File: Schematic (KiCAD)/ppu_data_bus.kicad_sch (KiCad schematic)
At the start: 72 parts, among them J65 Reg 4 D-Latch N, J68 Counter 4 Reset CL3

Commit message: Schematic Updates:  - Added all 10-bit CHR banking registers $5120 - $512B, including where all 10 bits come from when written.  - Added 8-bit CHR bank register $5202, which is the bank used when rendering the V-Split region.    + V-Split seems to always be 8-bit, 8kB bank regardless of CHR mode.  The wiki doesn't say that and I don't know for sure.  - Added decoding logic that activates the correct CHR bank for CHR A10, A11, A12 (corresponding to columns AV, AW, AX).  - Noted, AX15 activates $5202 CHR Bank for V-Split region.  AX16 activates CHR Bank from data stored in ExRAM for extended attributes.  Therefore, AX15 driven by AT1 High means we specifically are in v-split region, and not extended attribute mode.  With this knowledge, backtracking up the chain from AT1 to N14 sheds very useful insight what the 3-bit shift register at N11/N12/N13 is doing.  We now know that N14 goes low specifically for pattern table fetches when rendering the V-split region, and does not appear dual-purposed for extended attribute fetch sequencing.  This may seem rather subtle or unimportant, but it is a good advancement for higher level understanding what that mysterious shift register might be doing.
SVG Trace Updates:
 - Registers $5120, 5121, 5122, 5123 (first 4 CHR bank register), the outputs were labeled in reverse order.
 - Register $5130 (highest CHR bank bits), the outputs were labeled with backwards polarity.  The error was not having taken into account that the CPU data bus input to the latches came already inverted to begin with.
 - Still wrong: Cell AV7, 2-input NAND gate.  One of the inputs is missing and it logically should be driven by AS19 like the 4 cells to its direct right.  I can't quite make out how it makes that connection.
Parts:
- removed B100, B99, E47, F32, G20, H90: NOR_2, symbol MMC5:NOR_2
- removed B103, B105, C32, C34, C35, C37, C39, C40, E46, E48, F14, F15, F17, F22, F23, F24, F26, F27, F33, F34, F35, F36, F7.1, F8, F9, G95, H100, H101, H102, H103, H108, H89, H91, H99: INVERT, symbol MMC5:INVERT
- removed C31(a), C31(b): D-FF No Reset, symbol MMC5:D-FF_No_Reset
- removed C33, C38: NOR_3, symbol MMC5:NOR_3
- removed C36, C41: Unk 2to2, symbol MMC5:UNKNOWN_2to2
- removed E45, H92: NAND_2, symbol MMC5:NAND_2
- removed E53, J68: Counter 4 Reset CL3, symbol MMC5:Counter_4_Reset_CL3
- removed E68, F37, G85, J65: Reg 4 D-Latch N, symbol MMC5:Reg_4_D-Latch_N
- removed F10, F11, F12, F13, G93, G94, G98, G99: NAND_3, symbol MMC5:NAND_3
- removed F16, G97: NAND_4, symbol MMC5:NAND_4
- removed F18, F19, F20, F21, H104, H105, H106, H107: AOI_2, symbol MMC5:AOI_2
- added BH1, BH10, BH17, BH19, BH2, BH21, BH23, BH25, BH26, BH27, BH9, BK12, BK16, BK20, BK24, BK28, BK32, BK36, BK8, BL28, BL30, BL31, BL38, BL39, BL40, BL45: INVERT, symbol MMC5:INVERT
- added BH11, BH3: NAND_5, symbol MMC5:NAND_5
- added BH12, BH13, BH14, BH15, BH16, BH4, BH5, BH6, BH7, BH8, BK10, BK13, BK14, BK17, BK18, BK21, BK22, BK25, BK26, BK29, BK30, BK33, BK34, BK37, BK38, BK40, BK41, BK42, BK43, BK9, BL12, BL13, BL14, BL15, BL16, BL17, BL18, BL19, BL35, BL36, BL41, S2: NAND_2, symbol MMC5:NAND_2
- added BH18, BH20, BH22, BH24, BK11, BK15, BK19, BK23, BK27, BK31, BK35, BK7, BL32, BL37, BL42: NAND_3, symbol MMC5:NAND_3
- added BK1, BK39, BK44, BL1, BL10, BL2, BL3, BL34, BL4, BL46, BL5, BL6, BL7, S1: BUFFER, symbol MMC5:BUFFER
- added BL29: NAND_4, symbol MMC5:NAND_4
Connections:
- new net: BK24. (X), BK25. (X)
- new net: BK23. (X), BK24. (X)
- new net: BL12. (X), BL13. (X), BL14. (X), BL15. (X), BL16. (X), BL17. (X), BL18. (X), BL19. (X), BL31. (X)
- new net: BK15. (X), BL14. (X)
- new net: BL14. (X), BL2. (X)
- new net: BK10. (X), BK14. (X), BK18. (X), BK22. (X), BK26. (X), BK30. (X), BK34. (X), BK38. (X), BL39. (X)
- new net: BL39. (X), BL42. (X)
- new net: BL41. (X), BL45. (X)
- new net: BL41. (X), BL42. (X)
- new net: BH21. (X), BH22. (X)
- new net: BH12. (X), BH21. (X), BH4. (X)
- new net: BK8. (X), BK9. (X)
- new net: BK7. (X), BK8. (X)
- new net: BL31. (X), BL32. (X)
- new net: BH19. (X), BH20. (X)
- new net: BH14. (X), BH19. (X), BH6. (X)
- new net: BK25. (X), BK26. (X)
- new net: BH13. (X), BH23. (X), BH5. (X)
- new net: BH11. (X), BH13. (X)
- new net: BK35. (X), BL19. (X)
- new net: BL19. (X), BL7. (X)
- new net: BK10. (X), BK9. (X)
- new net: BL34. (X), BL35. (X), BL37. (X)
- new net: BL35. (X), BL40. (X)
- new net: BL29. (X), BL35. (X)
- new net: BK7. (X), BL12. (X)
- new net: BK1. (X), BL12. (X)
- new net: S1. (X), S2. (X)
- new net: BK15. (X), BK23. (X), BK31. (X), BK42. (X), BK7. (X)
- new net: BK15. (X), BK23. (X), BK31. (X), BK43. (X), BK7. (X)
- new net: BK31. (X), BL18. (X)
- new net: BK31. (X), BK32. (X)
- new net: BK37. (X), BK38. (X)
- new net: BK36. (X), BK37. (X)
- new net: BK15. (X), BK16. (X)
- new net: BK16. (X), BK17. (X)
- new net: BL45. (X), BL46. (X)
- new net: BH18. (X), BH20. (X), BH26. (X)
- new net: BH18. (X), BH20. (X), BH22. (X), BH24. (X), BH25. (X)
- new net: BH17. (X), BH18. (X)
- new net: BH18. (X), BH22. (X), BH27. (X)
- new net: BH15. (X), BH17. (X), BH7. (X)
- new net: BH11. (X), BH15. (X)
- new net: BK29. (X), BK30. (X)
- new net: BK28. (X), BK29. (X)
- new net: BK11. (X), BK19. (X), BK27. (X), BK35. (X), BK40. (X)
- new net: BK39. (X), BK40. (X), BK42. (X)
- new net: BH1. (X), BH2. (X)
- new net: BH2. (X), BH3. (X)
- new net: BK23. (X), BL16. (X)
- new net: BK11. (X), BK19. (X), BK27. (X), BK35. (X), BK41. (X)
- new net: BK11. (X), BL13. (X)
- new net: BK11. (X), BK12. (X)
- new net: BK21. (X), BK22. (X)
- new net: BH1. (X), BK41. (X)
- new net: BK12. (X), BK13. (X)
- new net: BK13. (X), BK14. (X)
- new net: BH10. (X), BH9. (X)
- new net: BH10. (X), BH11. (X)
- new net: BK39. (X), BL30. (X)
- new net: BL1. (X), BL13. (X)
- new net: BL28. (X), BL29. (X), BL37. (X)
- new net: BL18. (X), BL6. (X)
- new net: BL10. (X), BL34. (X)
- new net: BL15. (X), BL3. (X)
- new net: BL29. (X), BL30. (X)
- new net: BK27. (X), BL17. (X)
- new net: BK27. (X), BK28. (X)
- new net: BH23. (X), BH24. (X)
- new net: BH20. (X), BH24. (X), BH27. (X), S1. (X)
- new net: BK41. (X), BK43. (X), BK44. (X)
- new net: BL36. (X), BL37. (X)
- new net: BL37. (X), BL38. (X), BL42. (X)
- new net: BK20. (X), BK21. (X)
- new net: BK33. (X), BK34. (X)
- new net: BK44. (X), BL38. (X)
- new net: BH11. (X), BH16. (X)
- new net: BL17. (X), BL5. (X)
- new net: BK35. (X), BK36. (X)
- new net: BL16. (X), BL4. (X)
- new net: BK19. (X), BL15. (X)
- new net: BH3. (X), BH5. (X)
- new net: BH3. (X), BH8. (X)
- new net: BH3. (X), BH4. (X)
- new net: BH3. (X), BH7. (X)
- new net: BH3. (X), BH6. (X)
- new net: BK17. (X), BK18. (X)
- new net: BH9. (X), BK43. (X)
- new net: BK32. (X), BK33. (X)
- new net: BK19. (X), BK20. (X)
- new net: BH11. (X), BH14. (X)
- new net: BH11. (X), BH12. (X)
- new net +$5106.0_Fill_Mode_Tile{L11}: BK1. (X)
- new net +$5106.1_Fill_Mode_Tile{L12}: BL1. (X)
- new net +$5106.2_Fill_Mode_Tile{L14}: BL2. (X)
- new net +$5106.3_Fill_Mode_Tile{L13}: BL3. (X)
- new net +$5106.4_Fill_Mode_Tile{L18}: BL4. (X)
- new net +$5106.5_Fill_Mode_Tile{L17}: BL5. (X)
- new net +$5106.6_Fill_Mode_Tile{L16}: BL6. (X)
- new net +$5106.7_Fill_Mode_Tile{L15}: BL7. (X)
- new net +$5107.0_Fill_Mode_Color{BL8}: BK42. (X)
- new net +$5107.1_Fill_Mode_Color{BL9}: BK40. (X)
- new net +ExRAM_Nametable_Access{A9}: BL46. (X)
- new net +ExRAM_Read_D6_Latch{BJ11}: BH16. (X)
- new net +ExRAM_Read_D7_Latch{BJ11}: BH8. (X)
- new net +Fill_Mode_Nametable_Access{BL33}: BL29. (X), BL32. (X)
- new net +PPU_Fetch_Count.0{S10}: S2. (X)
- new net +PPU_Fetch_Count.1{S13}: S2. (X)
- new net +V-Split_Scanline_Counter.4{T22}: BH22. (X), BH24. (X), BH26. (X)
- new net ExRAM_D0_Read{BJ12(a)}: BH15. (X), BK10. (X)
- new net ExRAM_D1_Read{BJ12(b)}: BH7. (X), BK14. (X)
- new net ExRAM_D2_Read{BJ12(c)}: BH14. (X), BK18. (X)
- new net ExRAM_D3_Read{BJ12(d)}: BH6. (X), BK22. (X)
- new net ExRAM_D4_Read{BJ12(e)}: BH13. (X), BK26. (X)
- new net ExRAM_D5_Read{BJ12(f)}: BH5. (X), BK30. (X)
- new net ExRAM_D6_Read{BJ12(g)}: BH12. (X), BK34. (X)
- new net ExRAM_D7_Read{BJ12(h)}: BH4. (X), BK38. (X)
- new net PPU_D0_OUT_PIN: BK9. (X)
- new net PPU_D1_OUT_PIN: BK13. (X)
- new net PPU_D2_OUT_PIN: BK17. (X)
- new net PPU_D3_OUT_PIN: BK21. (X)
- new net PPU_D4_OUT_PIN: BK25. (X)
- new net PPU_D5_OUT_PIN: BK29. (X)
- new net PPU_D6_OUT_PIN: BK33. (X)
- new net PPU_D7_OUT_PIN: BK37. (X)
- new net PPU_RW_Mode_%0x_Access{BL48}: BL42. (X)
- new net V-Split_Side_Latched{BL43}: BH16. (X), BH25. (X), BH8. (X), BL29. (X), BL32. (X), BL36. (X), BL41. (X)
- new net /ExRAM_Mode_%01{BL49}: BL36. (X), BL40. (X)
- new net /PPU_Attribute_Access{BL25}: BL28. (X), BL32. (X)
- new net /Scanline_Counter_Reset{Z25}: BL10. (X)
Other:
- note added: "/Extended Attributes Enabled"
- note removed: "$5000 Register Pulse 1 Duty Envelope Volume"
- note removed: "$5004 Register Pulse 2 Duty Envelope Volume"
- note removed: "Bit 0 is internally bypassed."
- note removed: "Pulse 1 Duty Cycle Counter"
- note removed: "Pulse 1 Envelope/Volume Multiplexing"
- note removed: "Pulse 2 Duty Cycle Counter"
- note removed: "Pulse 2 Envelope/Volume Multiplexing"

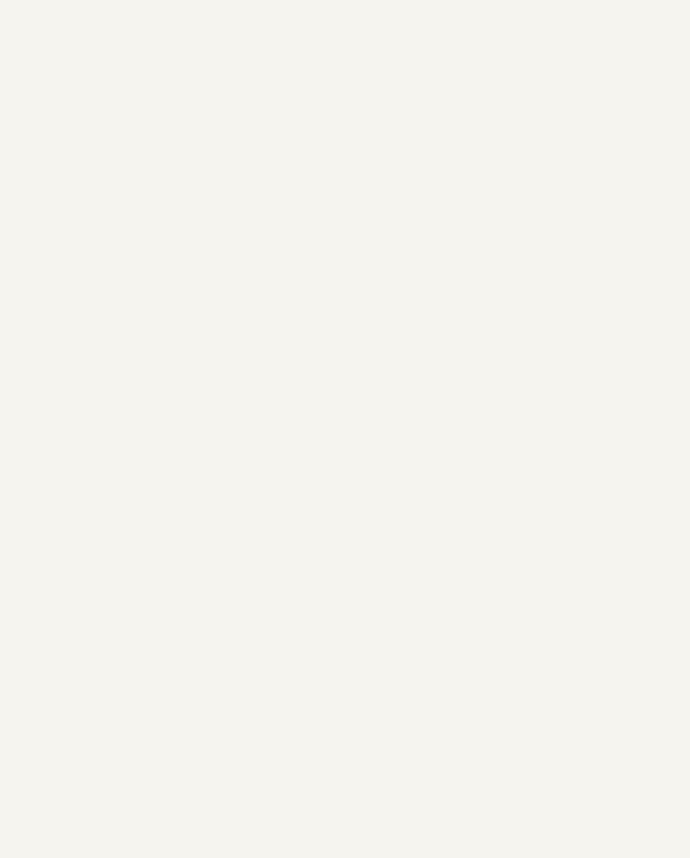
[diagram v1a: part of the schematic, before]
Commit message: - All cells in the left and center areas have now been added into the schematics.  - Changed naming of the PDF files; I was accidentally writing over furrtek's original with my new PDF.
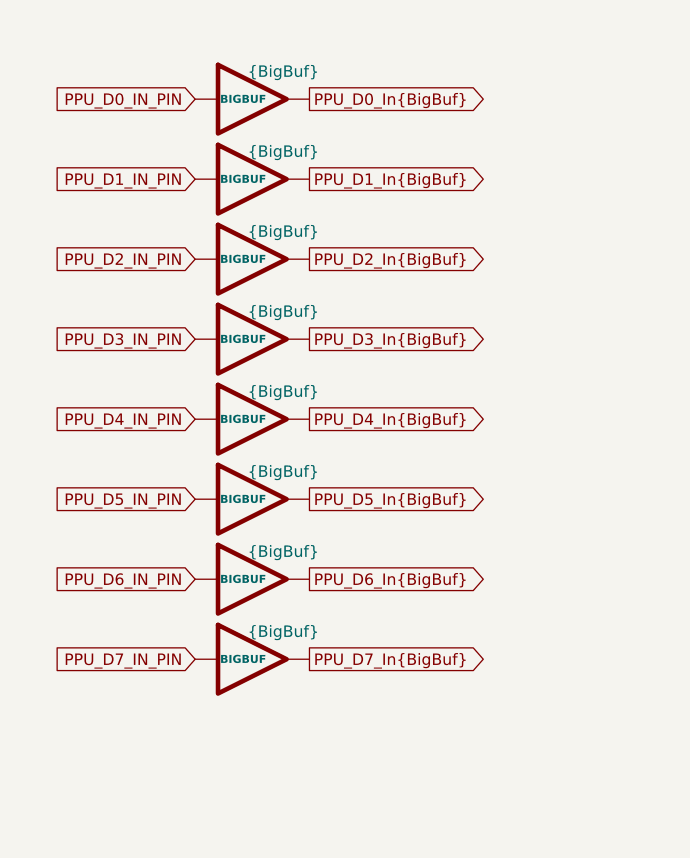
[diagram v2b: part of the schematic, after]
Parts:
- added {BigBuf} (x8): BIGBUF, symbol MMC5:BIGBUF
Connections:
- net at BK24. (X): now also BK23. (X); no longer BK25. (X)
- net at BK23. (X): now also BL16. (X); no longer BK24. (X)
- net at BL14. (X): now also BL2. (X); no longer BK15. (X)
- net at BL45. (X): now also BL46. (X); no longer BL41. (X)
- net at BH21. (X): now also BH12. (X), BH4. (X); no longer BH22. (X)
- net at BK8. (X): now also BK7. (X); no longer BK9. (X)
- net at BK7. (X): now also BK15. (X), BK23. (X), BK31. (X), BK43. (X); no longer BK8. (X)
- net at BH19. (X): now also BH14. (X), BH6. (X); no longer BH20. (X)
- net at BH11. (X): now also BH12. (X); no longer BH13. (X)
- net at BL19. (X): now also BL7. (X); no longer BK35. (X)
- net at BL35. (X): now also BL29. (X); no longer BL40. (X)
- net at BL12. (X): now also BK1. (X); no longer BK7. (X)
- net at S1. (X): now also BH20. (X), BH24. (X), BH27. (X); no longer S2. (X)
- net at BK31. (X): now also BK32. (X); no longer BL18. (X)
- net at BK32. (X): now also BK33. (X); no longer BK31. (X)
- net at BK36. (X): now also BK35. (X); no longer BK37. (X)
- net at BH18. (X): now also BH22. (X), BH27. (X); no longer BH17. (X)
- net at BK28. (X): now also BK27. (X); no longer BK29. (X)
- net at BH2. (X): now also BH3. (X); no longer BH1. (X)
- net at BH3. (X): now also BH6. (X); no longer BH2. (X)
- net at BL16. (X): now also BL4. (X); no longer BK23. (X)
- net at BK11. (X): now also BK12. (X); no longer BL13. (X)
- net at BK12. (X): now also BK13. (X); no longer BK11. (X)
- net at BH10. (X): now also BH11. (X); no longer BH9. (X)
- net at BL15. (X): now also BK19. (X); no longer BL3. (X)
- net at BL17. (X): now also BL5. (X); no longer BK27. (X)
- net at BL37. (X): now also BL38. (X), BL42. (X); no longer BL36. (X)
- net at BK20. (X): now also BK19. (X); no longer BK21. (X)
- new net: BK24. (X), BK25. (X)
- new net: BL12. (X), BL13. (X), BL14. (X), BL15. (X), BL16. (X), BL17. (X), BL18. (X), BL19. (X), BL31. (X)
- new net: BK15. (X), BL14. (X)
- new net: BK10. (X), BK14. (X), BK18. (X), BK22. (X), BK26. (X), BK30. (X), BK34. (X), BK38. (X), BL39. (X)
- new net: BL41. (X), BL45. (X)
- new net: BL41. (X), BL42. (X)
- new net: BH21. (X), BH22. (X)
- new net: BK8. (X), BK9. (X)
- new net: BH19. (X), BH20. (X)
- new net: BK25. (X), BK26. (X)
- new net: BH13. (X), BH23. (X), BH5. (X)
- new net: BH11. (X), BH13. (X)
- new net: BK35. (X), BL19. (X)
- new net: BK10. (X), BK9. (X)
- new net: BL34. (X), BL35. (X), BL37. (X)
- new net: BL35. (X), BL40. (X)
- new net: BK7. (X), BL12. (X)
- new net: S1. (X), S2. (X)
- new net: BK15. (X), BK23. (X), BK31. (X), BK42. (X), BK7. (X)
- new net: BK31. (X), BL18. (X)
- new net: BK37. (X), BK38. (X)
- new net: BK36. (X), BK37. (X)
- new net: BH18. (X), BH20. (X), BH26. (X)
- new net: BH18. (X), BH20. (X), BH22. (X), BH24. (X), BH25. (X)
- new net: BH17. (X), BH18. (X)
- new net: BH15. (X), BH17. (X), BH7. (X)
- new net: BH11. (X), BH15. (X)
- new net: BK29. (X), BK30. (X)
- new net: BK28. (X), BK29. (X)
- new net: BK11. (X), BK19. (X), BK27. (X), BK35. (X), BK40. (X)
- new net: BK39. (X), BK40. (X), BK42. (X)
- new net: BH1. (X), BH2. (X)
- new net: BK11. (X), BK19. (X), BK27. (X), BK35. (X), BK41. (X)
- new net: BK11. (X), BL13. (X)
- new net: BK21. (X), BK22. (X)
- new net: BK13. (X), BK14. (X)
- new net: BH10. (X), BH9. (X)
- new net: BL28. (X), BL29. (X), BL37. (X)
- new net: BL15. (X), BL3. (X)
- new net: BK27. (X), BL17. (X)
- new net: BK41. (X), BK43. (X), BK44. (X)
- new net: BL36. (X), BL37. (X)
- new net: BK20. (X), BK21. (X)
- new net: BK33. (X), BK34. (X)
- new net: BH11. (X), BH16. (X)
- new net: BH3. (X), BH5. (X)
- new net: BH3. (X), BH8. (X)
- new net: BH3. (X), BH4. (X)
- new net: BH3. (X), BH7. (X)
- new net: BK17. (X), BK18. (X)
- new net: BH11. (X), BH14. (X)
- new net PPU_D0_IN_PIN: {BigBuf}. (X)
- new net PPU_D0_In{BigBuf}: {BigBuf}. (X)
- new net PPU_D1_IN_PIN: {BigBuf}. (X)
- new net PPU_D1_In{BigBuf}: {BigBuf}. (X)
- new net PPU_D2_IN_PIN: {BigBuf}. (X)
- new net PPU_D2_In{BigBuf}: {BigBuf}. (X)
- new net PPU_D3_IN_PIN: {BigBuf}. (X)
- new net PPU_D3_In{BigBuf}: {BigBuf}. (X)
- new net PPU_D4_IN_PIN: {BigBuf}. (X)
- new net PPU_D4_In{BigBuf}: {BigBuf}. (X)
- new net PPU_D5_IN_PIN: {BigBuf}. (X)
- new net PPU_D5_In{BigBuf}: {BigBuf}. (X)
- new net PPU_D6_IN_PIN: {BigBuf}. (X)
- new net PPU_D6_In{BigBuf}: {BigBuf}. (X)
- new net PPU_D7_IN_PIN: {BigBuf}. (X)
- new net PPU_D7_In{BigBuf}: {BigBuf}. (X)

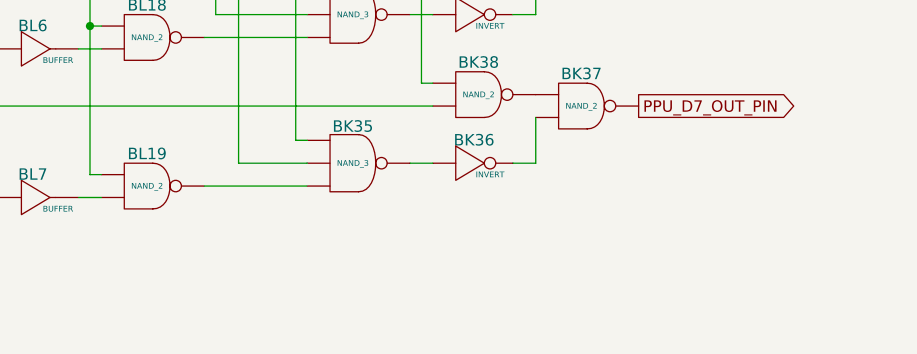
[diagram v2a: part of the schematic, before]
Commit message: - All known gates and traces are now accounted for in the schematics!  :)
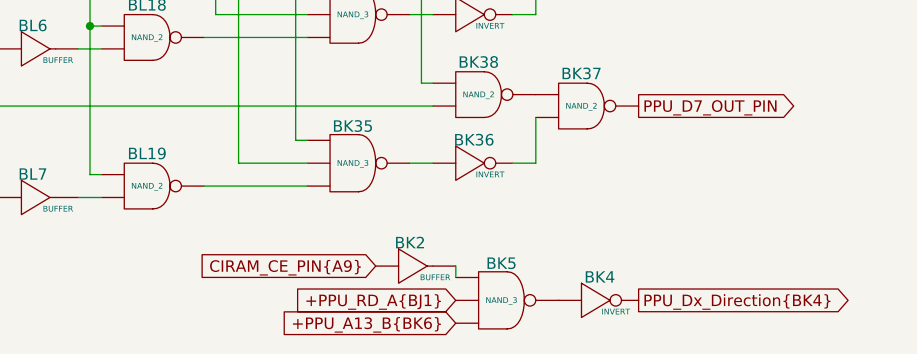
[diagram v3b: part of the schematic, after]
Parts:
- added BK2: BUFFER, symbol MMC5:BUFFER
- added BK4: INVERT, symbol MMC5:INVERT
- added BK5: NAND_3, symbol MMC5:NAND_3
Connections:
- net at BK24. (X): now also BK23. (X); no longer BK25. (X)
- net at BK23. (X): now also BL16. (X); no longer BK24. (X)
- net at BL14. (X): now also BL2. (X); no longer BK15. (X)
- net at BL45. (X): now also BL46. (X); no longer BL41. (X)
- net at BH21. (X): now also BH12. (X), BH4. (X); no longer BH22. (X)
- net at BK8. (X): now also BK7. (X); no longer BK9. (X)
- net at BK7. (X): now also BK15. (X), BK23. (X), BK31. (X), BK43. (X); no longer BK8. (X)
- net at BH19. (X): now also BH14. (X), BH6. (X); no longer BH20. (X)
- net at BH11. (X): now also BH12. (X); no longer BH13. (X)
- net at BL19. (X): now also BL7. (X); no longer BK35. (X)
- net at BL35. (X): now also BL29. (X); no longer BL40. (X)
- net at BL12. (X): now also BK1. (X); no longer BK7. (X)
- net at S1. (X): now also BH20. (X), BH24. (X), BH27. (X); no longer S2. (X)
- net at BK31. (X): now also BK32. (X); no longer BL18. (X)
- net at BK32. (X): now also BK33. (X); no longer BK31. (X)
- net at BK36. (X): now also BK35. (X); no longer BK37. (X)
- net at BH18. (X): now also BH22. (X), BH27. (X); no longer BH17. (X)
- net at BK28. (X): now also BK27. (X); no longer BK29. (X)
- net at BH2. (X): now also BH3. (X); no longer BH1. (X)
- net at BH3. (X): now also BH6. (X); no longer BH2. (X)
- net at BL16. (X): now also BL4. (X); no longer BK23. (X)
- net at BK11. (X): now also BK12. (X); no longer BL13. (X)
- net at BK12. (X): now also BK13. (X); no longer BK11. (X)
- net at BH10. (X): now also BH11. (X); no longer BH9. (X)
- net at BL15. (X): now also BK19. (X); no longer BL3. (X)
- net at BL17. (X): now also BL5. (X); no longer BK27. (X)
- net at BL37. (X): now also BL38. (X), BL42. (X); no longer BL36. (X)
- net at BK20. (X): now also BK19. (X); no longer BK21. (X)
- new net: BK24. (X), BK25. (X)
- new net: BL12. (X), BL13. (X), BL14. (X), BL15. (X), BL16. (X), BL17. (X), BL18. (X), BL19. (X), BL31. (X)
- new net: BK15. (X), BL14. (X)
- new net: BK10. (X), BK14. (X), BK18. (X), BK22. (X), BK26. (X), BK30. (X), BK34. (X), BK38. (X), BL39. (X)
- new net: BL41. (X), BL45. (X)
- new net: BL41. (X), BL42. (X)
- new net: BH21. (X), BH22. (X)
- new net: BK8. (X), BK9. (X)
- new net: BK4. (X), BK5. (X)
- new net: BK2. (X), BK5. (X)
- new net: BH19. (X), BH20. (X)
- new net: BK25. (X), BK26. (X)
- new net: BH13. (X), BH23. (X), BH5. (X)
- new net: BH11. (X), BH13. (X)
- new net: BK35. (X), BL19. (X)
- new net: BK10. (X), BK9. (X)
- new net: BL34. (X), BL35. (X), BL37. (X)
- new net: BL35. (X), BL40. (X)
- new net: BK7. (X), BL12. (X)
- new net: S1. (X), S2. (X)
- new net: BK15. (X), BK23. (X), BK31. (X), BK42. (X), BK7. (X)
- new net: BK31. (X), BL18. (X)
- new net: BK37. (X), BK38. (X)
- new net: BK36. (X), BK37. (X)
- new net: BH18. (X), BH20. (X), BH26. (X)
- new net: BH18. (X), BH20. (X), BH22. (X), BH24. (X), BH25. (X)
- new net: BH17. (X), BH18. (X)
- new net: BH15. (X), BH17. (X), BH7. (X)
- new net: BH11. (X), BH15. (X)
- new net: BK29. (X), BK30. (X)
- new net: BK28. (X), BK29. (X)
- new net: BK11. (X), BK19. (X), BK27. (X), BK35. (X), BK40. (X)
- new net: BK39. (X), BK40. (X), BK42. (X)
- new net: BH1. (X), BH2. (X)
- new net: BK11. (X), BK19. (X), BK27. (X), BK35. (X), BK41. (X)
- new net: BK11. (X), BL13. (X)
- new net: BK21. (X), BK22. (X)
- new net: BK13. (X), BK14. (X)
- new net: BH10. (X), BH9. (X)
- new net: BL28. (X), BL29. (X), BL37. (X)
- new net: BL15. (X), BL3. (X)
- new net: BK27. (X), BL17. (X)
- new net: BK41. (X), BK43. (X), BK44. (X)
- new net: BL36. (X), BL37. (X)
- new net: BK20. (X), BK21. (X)
- new net: BK33. (X), BK34. (X)
- new net: BH11. (X), BH16. (X)
- new net: BH3. (X), BH5. (X)
- new net: BH3. (X), BH8. (X)
- new net: BH3. (X), BH4. (X)
- new net: BH3. (X), BH7. (X)
- new net: BK17. (X), BK18. (X)
- new net: BH11. (X), BH14. (X)
- new net +PPU_A13_B{BK6}: BK5. (X)
- new net +PPU_RD_A{BJ1}: BK5. (X)
- new net CIRAM_CE_PIN{A9}: BK2. (X)
- new net PPU_Dx_Direction{BK4}: BK4. (X)
